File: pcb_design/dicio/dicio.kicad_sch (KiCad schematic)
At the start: 76 parts, among them J1 Conn_02x03_Counter_Clockwise, J2 Conn_01x06_Female, J3 USB_C_Receptacle, J4 Micro_SD_Card, J5 USB_C_Receptacle, J6 USB_C_Receptacle, J7 Conn_02x13_Odd_Even, J8 USB_C_Receptacle, Q1 Q_NMOS_GSD, SW1 SW_SPST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

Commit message: Improved design.
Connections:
- net C1TX: now also U1.51 (PMBE/RP67/RD3); no longer U1.27 (TCK/AN12/PMA11/RPI44/RB12)
- net OW3: now also U1.3 (AN31/PWM4H/PMD7/RP87/RE7); no longer U1.4 (C1IN3-/SCK2/PMA5/RP118/RG6)
- net U1TX: now also U1.4 (C1IN3-/SCK2/PMA5/RP118/RG6); no longer U1.3 (AN31/PWM4H/PMD7/RP87/RE7)
- no-connect marks 39 -> 38
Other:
- moved on the sheet: J3, J5, J6, J8, U1

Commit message: Update.
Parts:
- removed U1: dsPIC33EP256MU806, Package_QFP:TQFP-64_10x10mm_P0.5mm, symbol custom_components:dsPIC33EP256MU806
- added C28: 0.1uF, Capacitor_SMD:C_0603_1608Metric, symbol Device:C
- added R16: 10k, Capacitor_SMD:C_0603_1608Metric, symbol Device:R
- added U1: dsPIC33EP512MC806, Package_QFP:TQFP-64_10x10mm_P0.5mm, symbol custom_components:dsPIC33EP512MC806
- added U8: FT232RL, Package_SO:SSOP-28_5.3x10.2mm_P0.65mm, symbol Interface_USB:FT232RL
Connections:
- net AS1: now also J3.A7 (D-), J3.B7 (D-), U1.64 (AN28/PWM3L/PMD4/RP84/RE4); no longer J3.A10 (RX2-), J3.B10 (RX1-)
- net AS2: now also J5.A7 (D-), J5.B7 (D-), U1.14 (AN2/C2IN2-/VMIO/RPI34/RB2); no longer J5.A10 (RX2-), J5.B10 (RX1-)
- net AS3: now also J6.A7 (D-), J6.B7 (D-), U1.63 (AN27PWM2H/PMD3/RPI83/RE3); no longer J6.A10 (RX2-), J6.B10 (RX1-)
- net AS4: now also J8.A7 (D-), J8.B7 (D-), U1.16 (PGED3/AN0/VREF+/RPI32/RB0); no longer J8.A10 (RX2-), J8.B10 (RX1-)
- net BTN: now also U1.42 (RTCC/RPI72/RD8)
- net C1RX: now also U1.28 (TDI/AN13/PMA10/RPI45/RB13)
- net C1TX: now also U1.51 (PMBE/RP67/RD3)
- net CAN_C1: now also U1.24 (TDO/AN11/PMA12/RPI43/RB11)
- net CAN_C2: now also U1.23 (TMS/AN10/PMA13/RPI42/RB10)
- net D+: now also U8.15 (USBD+)
- net D-: now also U8.16 (USBD-)
- net EN_VA: now also U1.21 (AN8/PMA6/RPI40/RB8)
- net ERR: now also U1.36 (SDA1/RG3)
- net GND: now also C28.2, U1.20 (AVSS), U1.25 (VSS), U1.41 (VSS), U1.9 (VSS), U8.18 (GND), U8.21 (GND), U8.25 (AGND), U8.26 (TEST), U8.7 (GND)
- net MISO1: now also U1.54 (C3IN2-/RP70/RD6)
- net MOSI1: now also U1.46 (INT0/RP64/RD0)
- net OSC1: now also U1.39 (OSC1/RPI60/RC12)
- net OSC2: now also U1.40 (OSC2/CLKO/RC15)
- net OW1: now also J3.A6 (D+), J3.B6 (D+), U1.2 (AN30/PWM4L/PMD6/RPI86/RE6); no longer J3.A3 (TX1-), J3.B3 (TX2-)
- net OW2: now also J5.A6 (D+), J5.B6 (D+), U1.13 (AN3/C2IN1+/VPIO/RPI35/RB3); no longer J5.A3 (TX1-), J5.B3 (TX2-)
- net OW3: now also J6.A6 (D+), J6.B6 (D+), U1.3 (AN31/PWM4H/PMD7/RP87/RE7); no longer J6.A3 (TX1-), J6.B3 (TX2-)
- net OW4: now also J8.A6 (D+), J8.B6 (D+), U1.15 (PGEC3/AN1/VREF-/RPI33/RB1); no longer J8.A3 (TX1-), J8.B3 (TX2-)
- net PGC: now also U1.17 (PGEC1/AN6/RPI38/RB6)
- net PGD: now also U1.18 (PGED1/AN7/RPI39/RB7)
- net SCK1: now also U1.49 (RP65/RD1)
- net SCL1: now also J5.A10 (RX2-), J5.B10 (RX1-), J8.A10 (RX2-), J8.B10 (RX1-), U1.32 (SCL2/PMA8/RP101/RF5); no longer J5.A7 (D-), J5.B7 (D-), J8.A7 (D-), J8.B7 (D-)
- net SCL2: now also J3.A10 (RX2-), J3.B10 (RX1-), J6.A10 (RX2-), J6.B10 (RX1-), U1.44 (ASCL1/PMCS2/RPI74/RD10); no longer J3.A7 (D-), J3.B7 (D-), J6.A7 (D-), J6.B7 (D-)
- net SDA1: now also J5.A3 (TX1-), J5.B3 (TX2-), J8.A3 (TX1-), J8.B3 (TX2-), U1.31 (SDA2/PMA9/RP100/RF4); no longer J5.A6 (D+), J5.B6 (D+), J8.A6 (D+), J8.B6 (D+)
- net SDA2: now also J3.A3 (TX1-), J3.B3 (TX2-), J6.A3 (TX1-), J6.B3 (TX2-), U1.43 (ASDA1/RPI73/RD9); no longer J3.A6 (D+), J3.B6 (D+), J6.A6 (D+), J6.B6 (D+)
- net SI: now also U1.60 (AN24/PWM1L/PMD0/RP80/RE0)
- net SO: now also U1.59 (RP97/RF1)
- net SOSC1: now also U1.47 (PGED2/SOSCI/C3IN3-/RPI61/RC13)
- net SOSC2: now also U1.48 (PGEC2/SOSCO/C3IN1-/T1CK/RPI62/RC14)
- net SQICLK: now also U1.55 (C3IN1+/RP71/RD7)
- net SYNC: now also U1.22 (AN9/PMA7/RPI41/RB9)
- net S_PS_SW: now also U1.11 (AN5/C1IN1+/RPI37/RB5)
- net TERM: now also U1.29 (AN14/PMA1/RPI46/RB14)
- net U1RX: now also U1.6 (C2IN3-/SDO2/PMA3/RP120/RG8)
- net U1TX: now also U1.4 (C1IN3-/SCK2/PMA5/RP118/RG6)
- net VBUS: now also R16.1, U8.20 (VCC)
- net VCAP: now also U1.56 (VCAP)
- net VDDA: now also U1.19 (AVDD)
- net ~{CS_SD}: now also U1.45 (PMCS1/RPI75/RD11)
- net ~{HOLD}: now also U1.61 (AN25/PWM1H/PMD1/RPI81/RE1)
- net ~{INT1}: now also U1.12 (AN4/C1IN2-/RPI36/RB4)
- net ~{INT2}: now also U1.62 (AN26/PWM2L/PMD2/RP82/RE2)
- net ~{MCLR_w}: now also U1.7 (~{MCLR})
- net ~{RESET_M}: now also U1.58 (RP96/RF0)
- net ~{SQICS0}: now also U1.52 (PWMR/RP68/RD4)
- net ~{SQICS1}: now also U1.53 (PMRD/RP69/RD5)
- net ~{U1CTS}: now also U1.5 (C1IN1-/SDI2/PMA4/RPI119/RG7)
- net ~{U1RTS}: now also U1.1 (AN29/PWM3H/PMD5/RP85/RE5)
- net ~{WP}: now also U1.30 (AN15/PMA0/RPI47/RB15)
- net +3V3 renamed +3.3V
- net +3.3V: now also U1.10 (VDD), U1.26 (VDD), U1.38 (VDD), U1.57 (VDD), U8.4 (VCCIO)
- new net: C28.1, U8.17 (3V3OUT)
- new net: R16.2, U8.19 (~{RESET})
- new net USB_CTS: U1.27 (TCK/AN12/PMA11/RPI44/RB12), U8.3 (RTS)
- new net USB_RTS: U1.35 (RP102/RF6), U8.11 (CTS)
- new net USB_RX: U1.33 (RP99/RF3), U8.5 (RXD)
- new net USB_TX: U1.34 (RP98/RF2), U8.1 (TXD)
- no-connect marks 38 -> 50
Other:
- note removed: "I2C sensor"
- note removed: "One Wire sensor"
- note removed: "analogue sensor connection"
- note removed: "analogue sensor power supply"
- note removed: "differential analogue sensor"
- note removed: "sensor interrupt"

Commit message: Updated files.
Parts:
- R16: footprint Capacitor_SMD:C_0603_1608Metric -> Resistor_SMD:R_0603_1608Metric
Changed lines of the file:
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@@
     (property "Reference" "R16" (id 0) (at 44.45 344.17 90))
     (property "Value" "10k" (id 1) (at 44.45 346.71 90))
-    (property "Footprint" "Capacitor_SMD:C_0603_1608Metric" (id 2) (at 44.45 352.298 90)
+    (property "Footprint" "Resistor_SMD:R_0603_1608Metric" (id 2) (at 44.45 352.298 90)
       (effects (font (size 1.27 1.27)) hide)
     )
@@
     )
     (path "/c4009b0c-278e-45a9-b639-af3372bb175b"
-      (reference "R16") (unit 1) (value "10k") (footprint "Capacitor_SMD:C_0603_1608Metric")
+      (reference "R16") (unit 1) (value "10k") (footprint "Resistor_SMD:R_0603_1608Metric")
     )
     (path "/00000000-0000-0000-0000-00005def4677"

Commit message: New and updated board designs.
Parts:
- removed J1: Conn_02x03_Counter_Clockwise, Connector_PinSocket_2.54mm:PinSocket_2x03_P2.54mm_Vertical, symbol Connector_Generic:Conn_02x03_Counter_Clockwise
- removed J7: Conn_02x13_Odd_Even, Connector_PinHeader_2.54mm:PinHeader_2x13_P2.54mm_Vertical, symbol Connector_Generic:Conn_02x13_Odd_Even
- added J1: Conn_02x10_Odd_Even, samtec:SAMTEC_TMMH-110-01-T-DV, symbol Connector_Generic:Conn_02x10_Odd_Even
- N1: footprint custom_footprints:Enclosure-Gloxinia2 -> custom_footprints:Enclosure-Gloxinia4
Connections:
- net +3.3V: now also J1.10 (Pin_10)
- net CAN_C1: now also J1.13 (Pin_13)
- net CAN_C2: now also J1.15 (Pin_15)
- net CAN_H: now also J1.3 (Pin_3)
- net CAN_L: now also J1.5 (Pin_5)
- net CC1: now also J1.18 (Pin_18)
- net D+: now also J1.17 (Pin_17)
- net D-: now also J1.19 (Pin_19)
- net GND: now also J1.7 (Pin_7), J1.9 (Pin_9)
- net SYNC: now also J1.12 (Pin_12)
- net U1RX: now also J1.8 (Pin_8)
- net U1TX: now also J1.6 (Pin_6)
- net VBUS: now also J1.1 (Pin_1)
- net VCONN: now also J1.20 (Pin_20)
- net V_USBC: now also J1.11 (Pin_11)
- net ~{U1CTS}: now also J1.4 (Pin_4)
- net ~{U1RTS}: now also J1.2 (Pin_2)
- no-connect marks 50 -> 43

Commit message: Expose RTCC pin for synchronisation
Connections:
- net BTN: now also J1.14 (Pin_14)
- no-connect marks 43 -> 42
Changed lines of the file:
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@@
   (junction (at 478.155 224.155) (diameter 0) (color 0 0 0 0)
   )
-  (no_connect (at 62.23 182.88))
   (no_connect (at 268.605 377.825))
   (no_connect (at 445.77 41.91))
@@
     (stroke (width 0) (type default) (color 0 0 0 0))
   )
+  (wire (pts (xy 62.23 182.88) (xy 72.39 182.88))
+    (stroke (width 0) (type default) (color 0 0 0 0))
+  )
   (wire (pts (xy 72.39 190.5) (xy 62.23 190.5))
     (stroke (width 0) (type default) (color 0 0 0 0))
@@
     (effects (font (size 1.27 1.27)) (justify right bottom))
   )
+  (label "BTN" (at 72.39 182.88 180)
+    (effects (font (size 1.27 1.27)) (justify right bottom))
+  )

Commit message: Change some component sizes
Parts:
- C23: footprint Capacitor_SMD:C_1206_3216Metric -> Capacitor_SMD:C_1210_3225Metric
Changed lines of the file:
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@@
       (effects (font (size 1.27 1.27)) (justify left))
     )
-    (property "Footprint" "Capacitor_SMD:C_1206_3216Metric" (id 2) (at 281.6352 56.896 0)
+    (property "Footprint" "Capacitor_SMD:C_1210_3225Metric" (id 2) (at 281.6352 56.896 0)
       (effects (font (size 1.27 1.27)) hide)
     )
@@
     )
     (path "/fbbb808d-778e-4398-a312-aedbff2b6c0e"
-      (reference "C23") (unit 1) (value "10uF") (footprint "Capacitor_SMD:C_1206_3216Metric")
+      (reference "C23") (unit 1) (value "10uF") (footprint "Capacitor_SMD:C_1210_3225Metric")
     )
     (path "/00000000-0000-0000-0000-00005ddd282f"

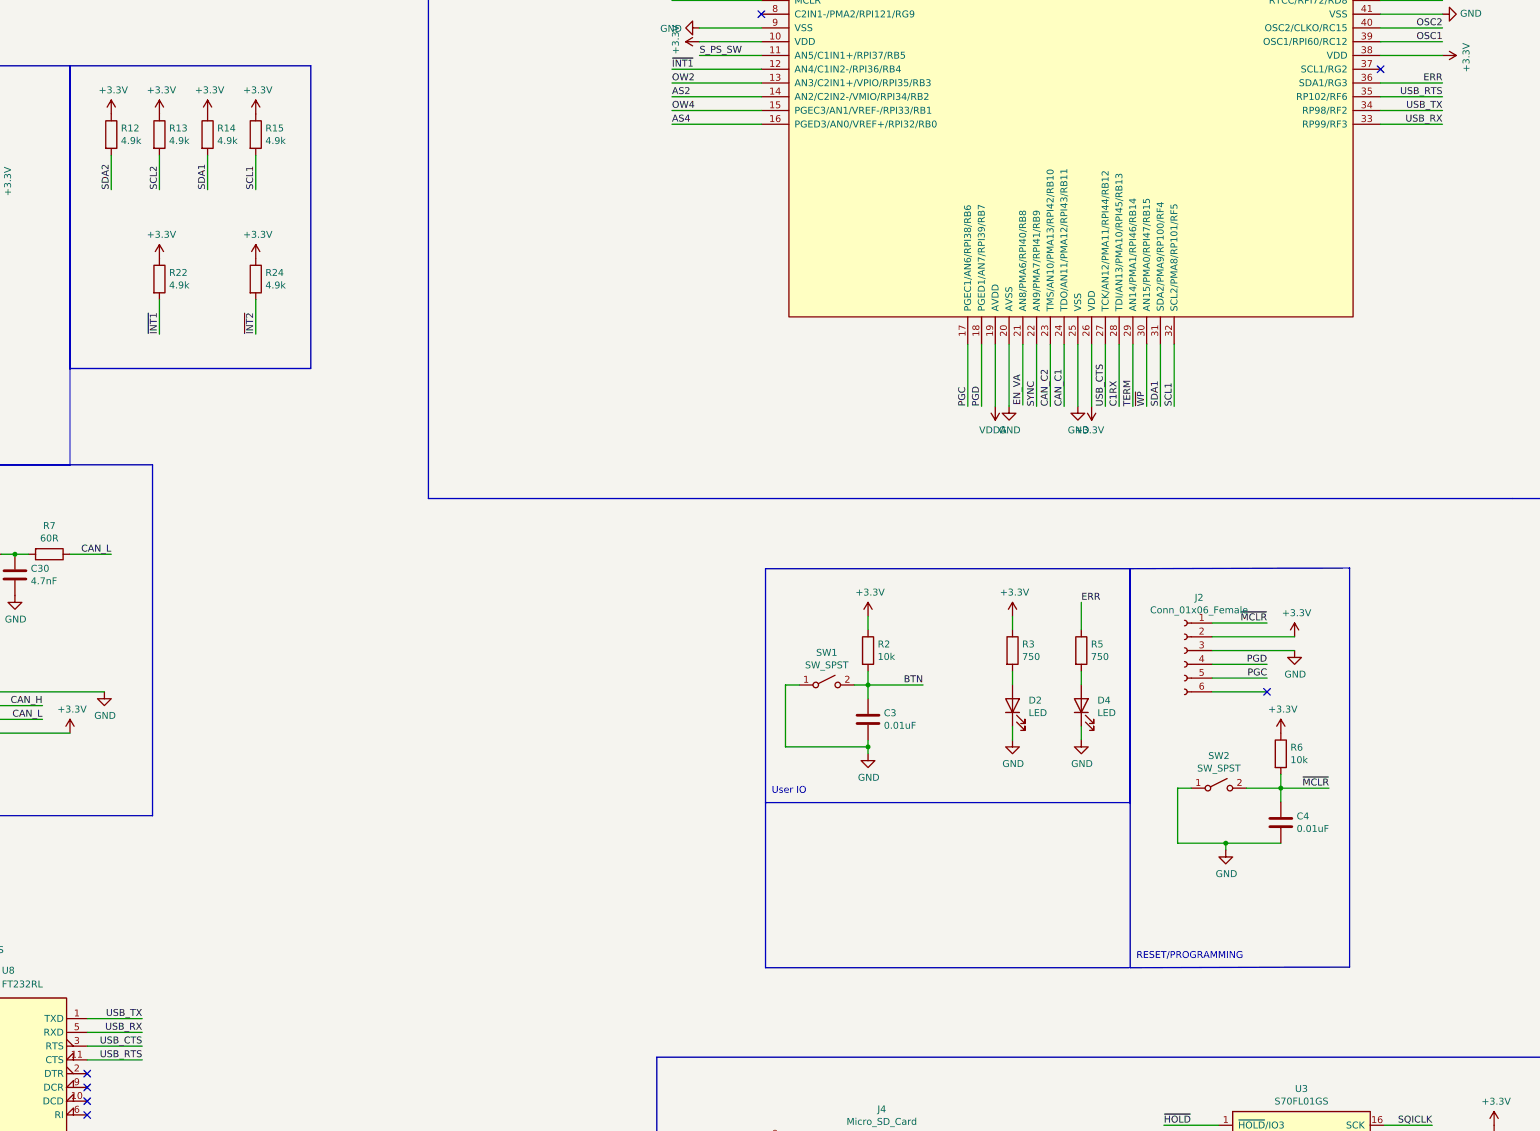
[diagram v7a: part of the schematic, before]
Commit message: Fix issue with labeling.
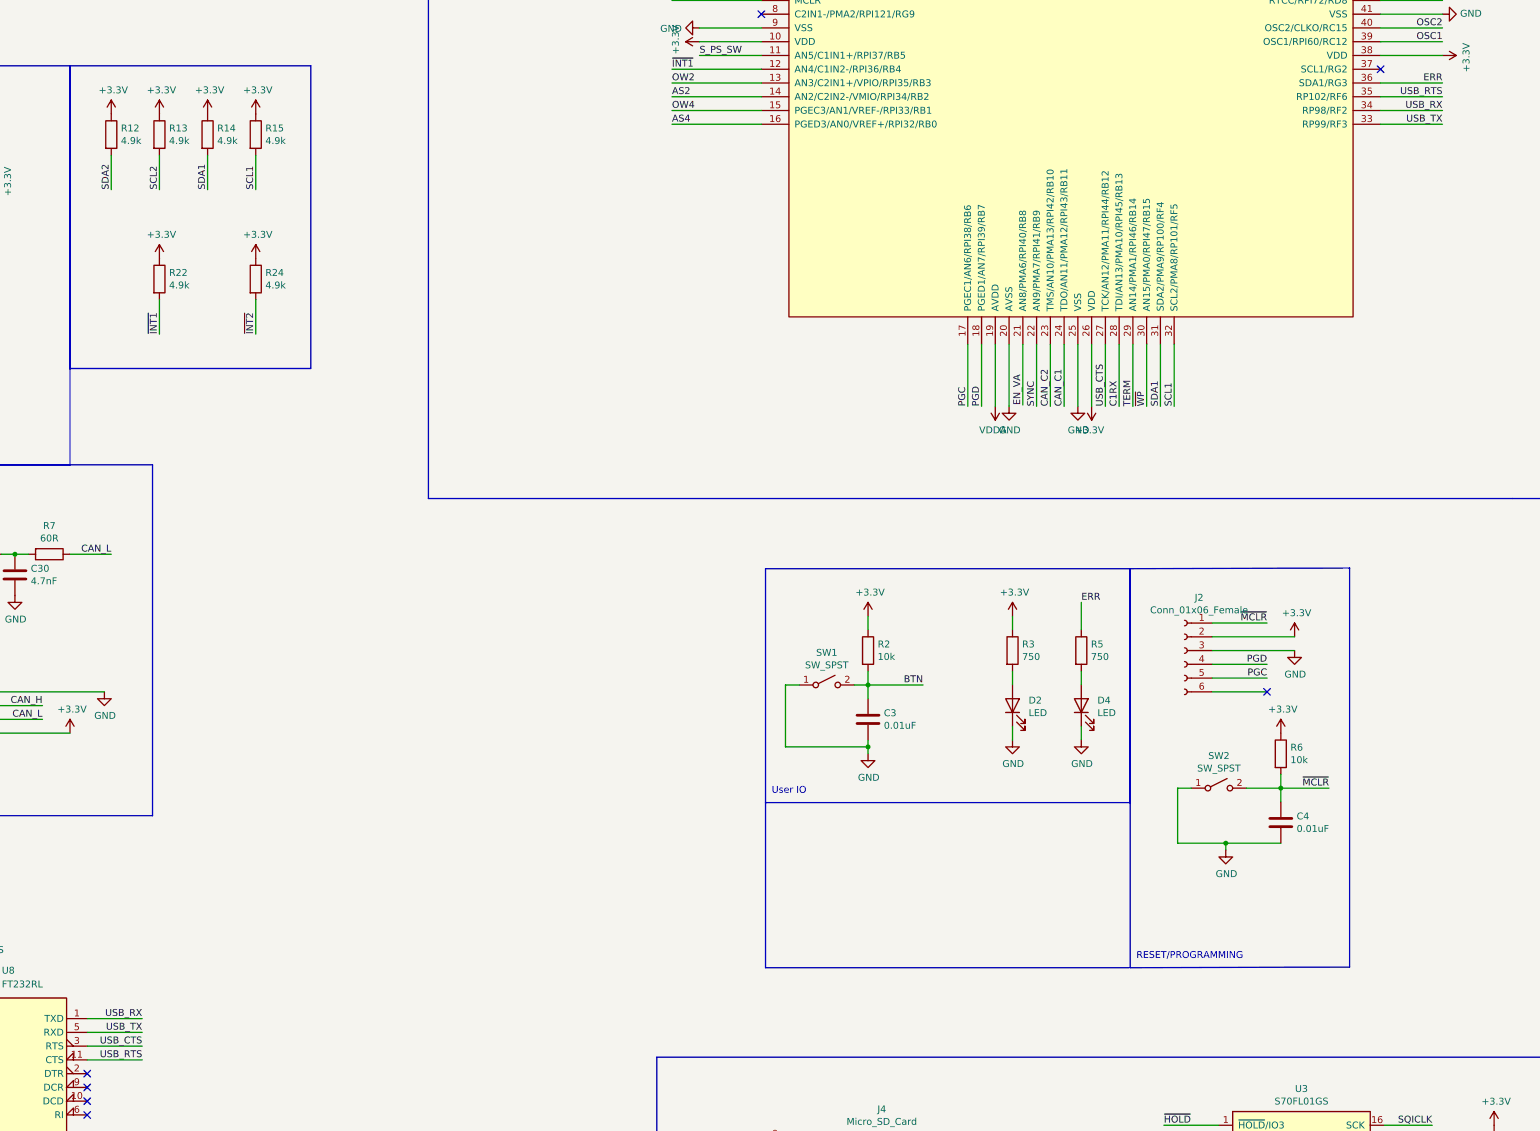
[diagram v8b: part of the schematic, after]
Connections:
- net USB_RX: now also U1.34 (RP98/RF2), U8.1 (TXD); no longer U1.33 (RP99/RF3), U8.5 (RXD)
- net USB_TX: now also U1.33 (RP99/RF3), U8.5 (RXD); no longer U1.34 (RP98/RF2), U8.1 (TXD)
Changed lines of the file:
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@@
     (effects (font (size 1.27 1.27)) (justify right bottom))
   )
-  (label "USB_TX" (at 101.6 332.74 180)
+  (label "USB_TX" (at 101.6 335.28 180)
     (effects (font (size 1.27 1.27)) (justify right bottom))
   )
@@
     (effects (font (size 1.27 1.27)) (justify right bottom))
   )
-  (label "USB_TX" (at 341.63 165.1 180)
+  (label "USB_TX" (at 341.63 167.64 180)
     (effects (font (size 1.27 1.27)) (justify right bottom))
   )
@@
     (effects (font (size 1.27 1.27)) (justify right bottom))
   )
-  (label "USB_RX" (at 101.6 335.28 180)
+  (label "USB_RX" (at 101.6 332.74 180)
     (effects (font (size 1.27 1.27)) (justify right bottom))
   )
@@
     (effects (font (size 1.27 1.27)) (justify right bottom))
   )
-  (label "USB_RX" (at 341.63 167.64 180)
-    (effects (font (size 1.27 1.27)) (justify right bottom))
-  )
+  (label "USB_RX" (at 341.63 165.1 180)
+    (effects (font (size 1.27 1.27)) (justify right bottom))
+  )
